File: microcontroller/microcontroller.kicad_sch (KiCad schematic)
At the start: 46 parts, among them J1 Conn_01x05_Pin, J2 Conn_01x10_Pin, J3 USB_C_Receptacle, J4 Conn_01x04_Pin, SW1 SW_SPST, SW2 SW_SPST, SW3 SW_SPST, U1 DS3231MZ, U2 AMS1117-3.3, U3 STM32F103CBTx, Y1 8Mhz

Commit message: Changed connectors
Changed connector from mcu to power supply to idc.
All switches now use a straight pinheader, with no pullups (now using
mcu pulldowns).
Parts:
- removed J1: Conn_01x05_Pin, Connector_PinHeader_2.54mm:PinHeader_1x05_P2.54mm_Vertical, symbol Connector:Conn_01x05_Pin
- removed R1, R2, R3: 10k, Resistor_SMD:R_0603_1608Metric, symbol Device:R
- removed SW1, SW2, SW3: SW_SPST, Connector_PinHeader_2.54mm:PinHeader_1x02_P2.54mm_Vertical, symbol Switch:SW_SPST
- added J1, J2: Conn_01x04_Pin, Connector_PinHeader_2.54mm:PinHeader_1x04_P2.54mm_Vertical, symbol Connector:Conn_01x04_Pin
- J3: renamed from J2; footprint Connector_PinHeader_2.54mm:PinHeader_1x10_P2.54mm_Vertical -> Connector_IDC:IDC-Header_2x05_P2.54mm_Vertical
- renumbered J3 to J4, J4 to J5, R4 to R1, R5 to R2, R6 to R3, R7 to R4, R8 to R5, R9 to R6, R10 to R7, R11 to R8, R12 to R9
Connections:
- net +3V3: now also J1.4 (Pin_4), J2.4 (Pin_4)
- net ADJUST_SW: now also U3.18 (PB0), J1.1 (Pin_1); no longer U3.13 (PA3)
- net HOUR_SW_H: now also U3.15 (PA5), J2.3 (Pin_3); no longer U3.16 (PA6)
- net MINUTE_SW_H: now also U3.14 (PA4), J2.2 (Pin_2); no longer U3.17 (PA7)
- net MODE_SW: now also U3.17 (PA7), J1.2 (Pin_2); no longer U3.14 (PA4)
- net POWER_SW: now also U3.16 (PA6), J1.3 (Pin_3); no longer U3.15 (PA5)
- net SECOND_SW_H: now also U3.13 (PA3), J2.1 (Pin_1); no longer U3.18 (PB0)
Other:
- note added: "To toggle switch breakout pcb"
- note added: "Use STM32F1 internal pulldown for switches"
- note removed: "TOGGLE SWITCHES"
- note removed: "These are panel mounted"

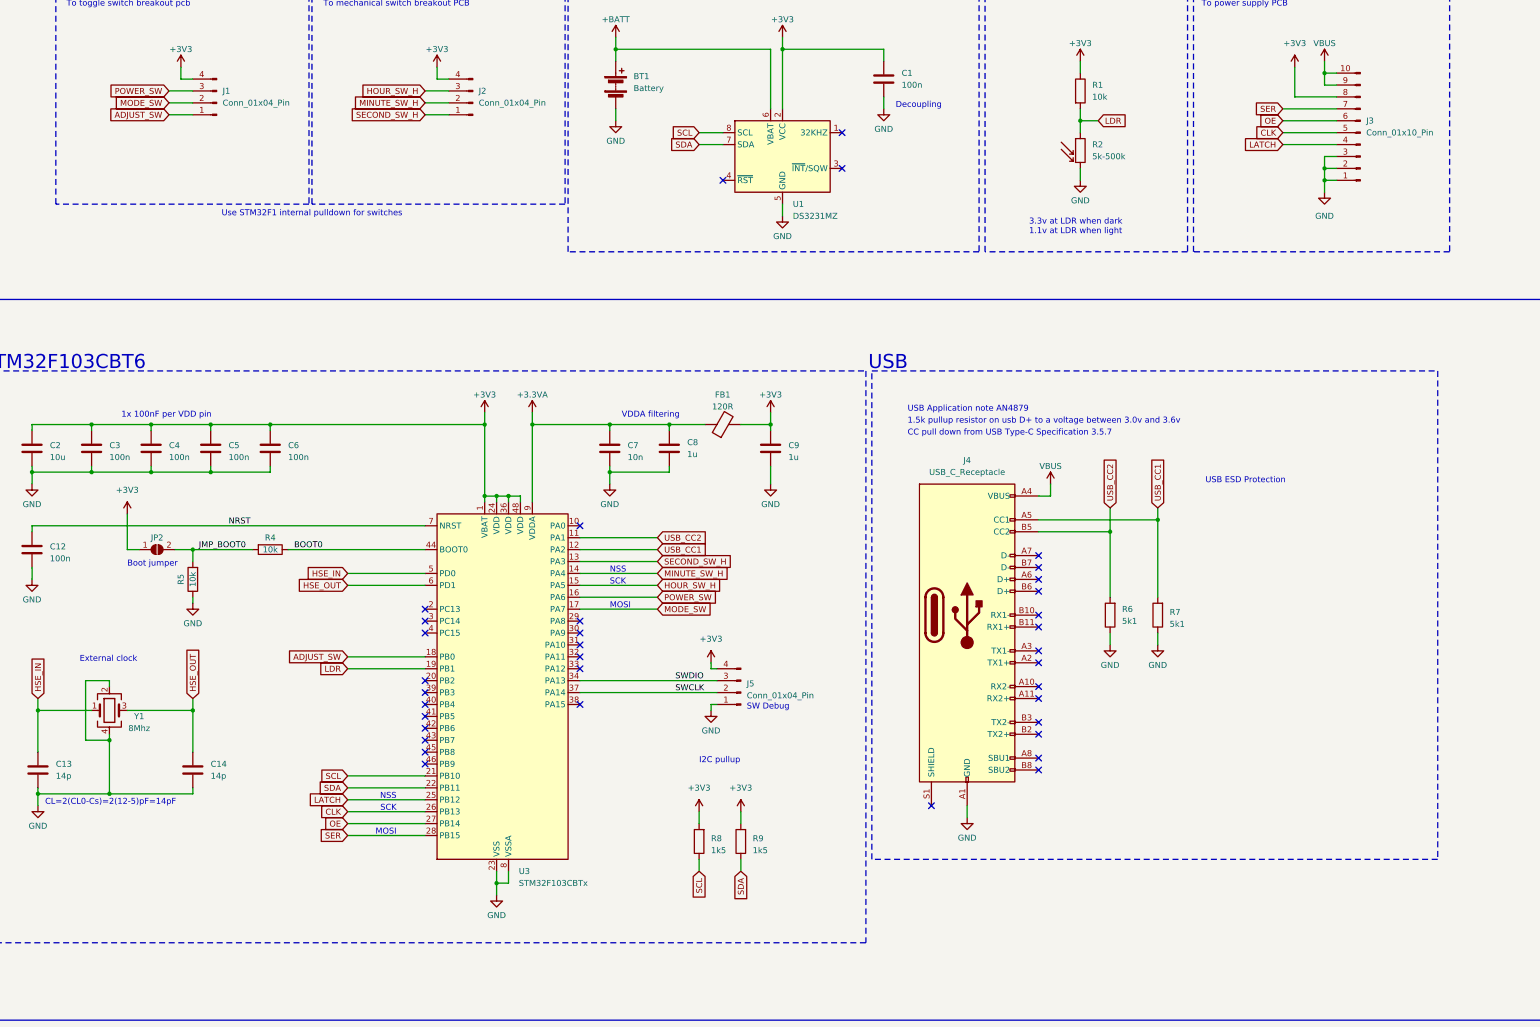
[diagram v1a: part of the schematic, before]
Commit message: Added ESD protection
Added esd protection to the mcu board.
Also added breakout board for panel mounted switches.
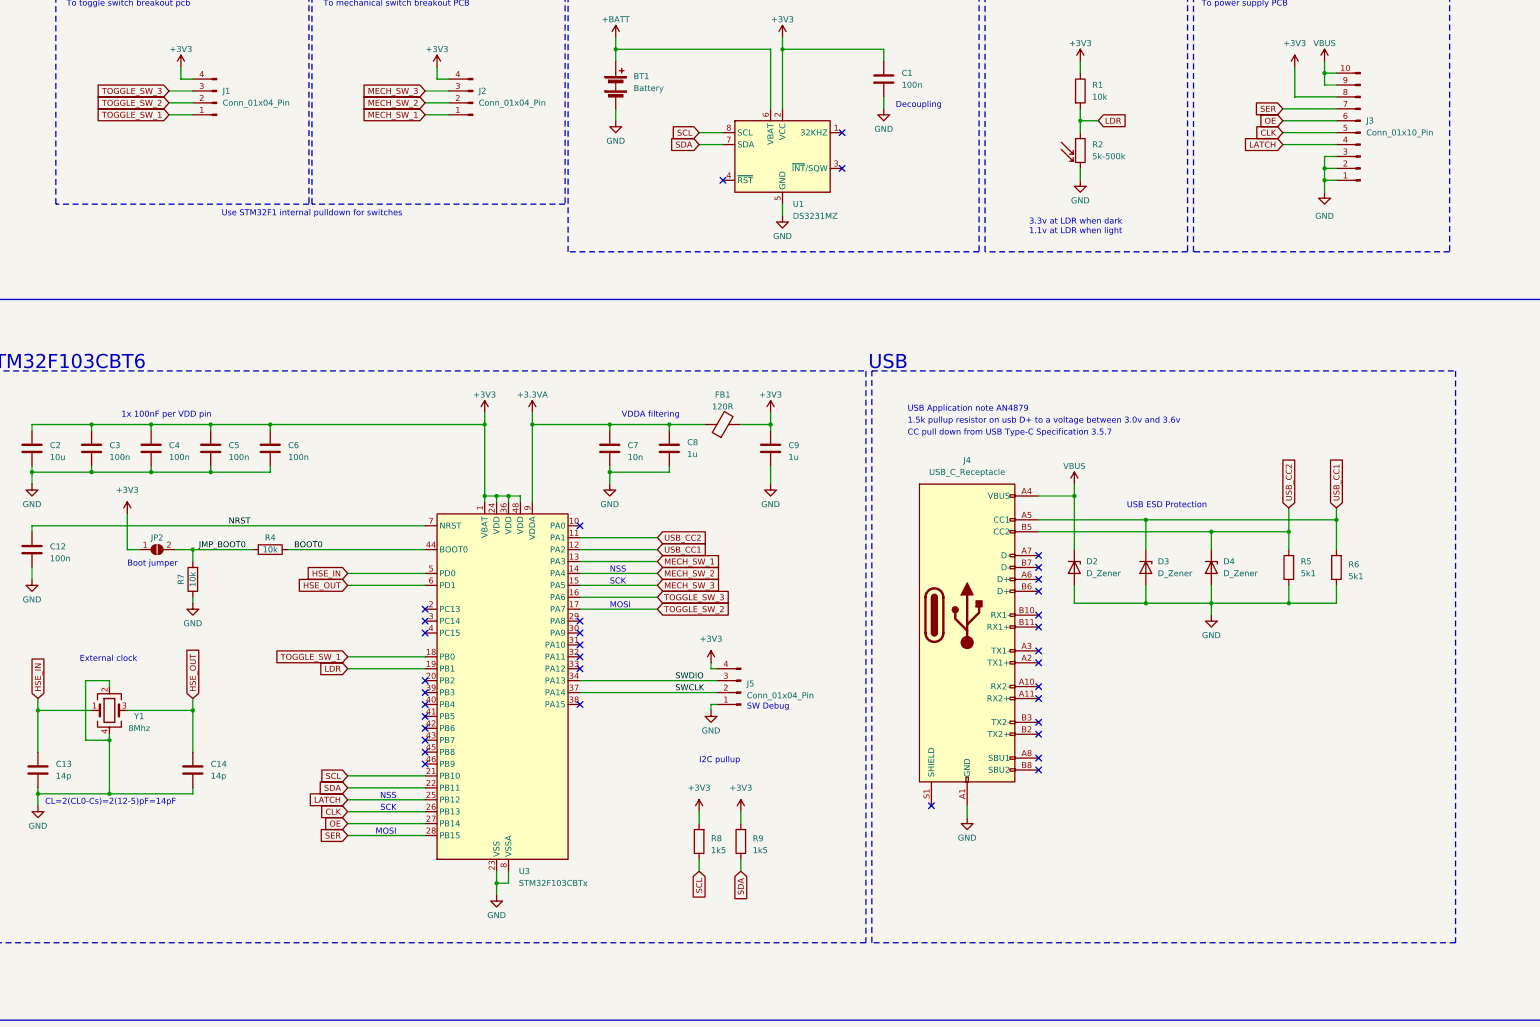
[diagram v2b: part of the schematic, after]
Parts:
- added D2, D3, D4: D_Zener, Diode_SMD:D_SOD-323, symbol Device:D_Zener
- renumbered R6 to R5, R7 to R6, R5 to R7
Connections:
- net GND: now also D2.2 (A), D3.2 (A), D4.2 (A)
- net USB_CC1: now also D3.1 (K)
- net USB_CC2: now also D4.1 (K)
- net VBUS: now also D2.1 (K)
- net ADJUST_SW renamed TOGGLE_SW_1
- net HOUR_SW_H renamed MECH_SW_3
- net MINUTE_SW_H renamed MECH_SW_2
- net MODE_SW renamed TOGGLE_SW_2
- net POWER_SW renamed TOGGLE_SW_3
- net SECOND_SW_H renamed MECH_SW_1
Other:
- moved on the sheet: R5, R6

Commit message: Changed main PCB mount
Changed nixie board pcb mount, so now screws are visible on the front
side of the board instead of the back. Also changed mcu i2c pullups to
2k2.
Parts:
- FB1: footprint Inductor_SMD:L_0603_1608Metric -> Resistor_SMD:R_0603_1608Metric
- R1: renamed from R3; value 1k5 -> 2k2
- R6: renamed from R8; value 1k5 -> 2k2
- R7: renamed from R9; value 1k5 -> 2k2
- renumbered C2 to C1, C11 to C10, C12 to C11, C13 to C12, C14 to C13, C1 to C14, C3 to C2, C4 to C3, C5 to C4, C6 to C5, C7 to C6, C8 to C7, C9 to C8, C10 to C9, J4 to J1, J5 to J2, J1 to J3, J2 to J4, J3 to J5, R4 to R2, R5 to R3, R6 to R4, R7 to R5, R1 to R8, R2 to R9, U2 to U1, U3 to U2, U1 to U3
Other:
- note removed: "1.5k pullup resistor on usb D+ to a voltage between 3.0v and 3.6v"
- note removed: "CC pull down from USB Type-C Specification 3.5.7"
- note removed: "USB Application note AN4879"
- moved on the sheet: BT1, C1, C10, C11, C12, C13, C14, C2, C3, C4, C5, C6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
